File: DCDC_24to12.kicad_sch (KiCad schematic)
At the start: 26 parts, among them J1 Power_IN, J2 Power_OUT, U1 BD9F800MUX-ZE2

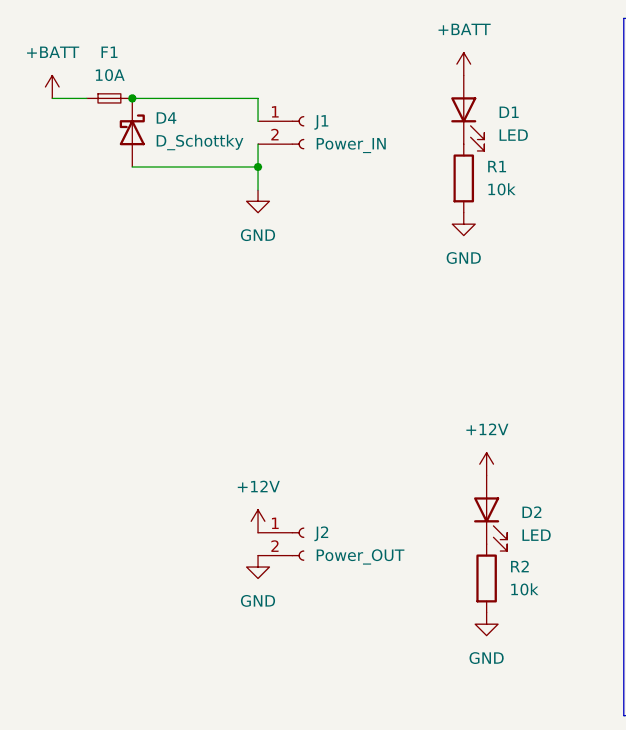
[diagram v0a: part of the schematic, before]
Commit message: XT60をヨコに変更、ピン順序修正
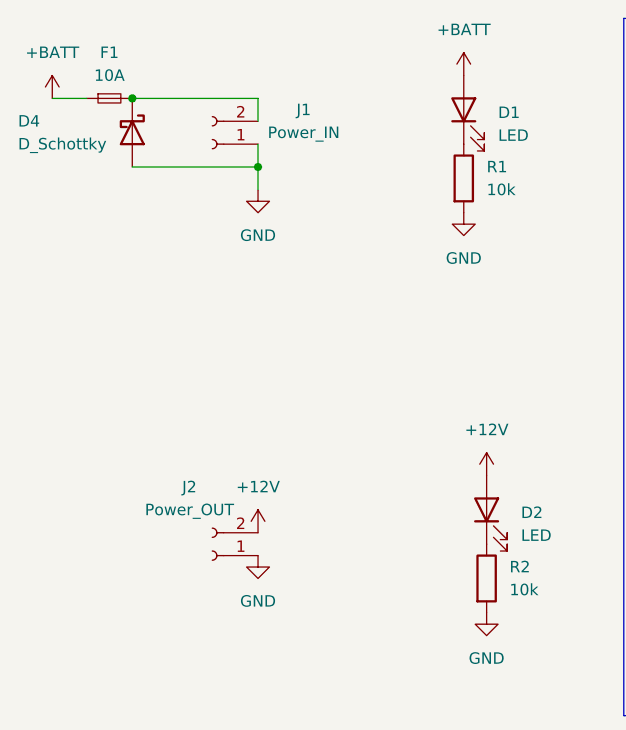
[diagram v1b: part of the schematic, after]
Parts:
- J1: footprint Connector_AMASS:AMASS_XT60-M_1x02_P7.20mm_Vertical -> Connector_AMASS:AMASS_XT60PW-M_1x02_P7.20mm_Horizontal
- J2: footprint Connector_AMASS:AMASS_XT60-F_1x02_P7.20mm_Vertical -> Connector_AMASS:AMASS_XT60PW-F_1x02_P7.20mm_Horizontal
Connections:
- net +12V: now also J2.2 (Pin_2); no longer J2.1 (Pin_1)
- net GND: now also J1.1 (Pin_1), J2.1 (Pin_1); no longer J1.2 (Pin_2), J2.2 (Pin_2)
- net at D4.1 (K), F1.2: now also J1.2 (Pin_2); no longer J1.1 (Pin_1)
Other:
- moved on the sheet: J1, J2
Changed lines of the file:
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@@
 	(symbol
 		(lib_id "Connector:Conn_01x02_Socket")
-		(at 50.8 78.74 0)
-		(unit 1)
-		(exclude_from_sim no)
-		(in_bom yes)
-		(on_board yes)
-		(dnp no)
-		(fields_autoplaced yes)
+		(at 40.64 81.28 180)
+		(unit 1)
+		(exclude_from_sim no)
+		(in_bom yes)
+		(on_board yes)
+		(dnp no)
 		(property "Reference" "J1"
-			(at 52.07 78.7399 0)
-			(effects
-				(font
-					(size 1.27 1.27)
-				)
-				(justify left)
+			(at 50.8 77.47 0)
+			(effects
+				(font
+					(size 1.27 1.27)
+				)
 			)
 		)
 		(property "Value" "Power_IN"
-			(at 52.07 81.2799 0)
-			(effects
-				(font
-					(size 1.27 1.27)
-				)
-				(justify left)
-			)
-		)
-		(property "Footprint" "Connector_AMASS:AMASS_XT60-M_1x02_P7.20mm_Vertical"
-			(at 50.8 78.74 0)
+			(at 50.8 80.01 0)
+			(effects
+				(font
+					(size 1.27 1.27)
+				)
+			)
+		)
+		(property "Footprint" "Connector_AMASS:AMASS_XT60PW-M_1x02_P7.20mm_Horizontal"
+			(at 40.64 81.28 0)
 			(effects
 				(font
@@
 		)
 		(property "Datasheet" "~"
-			(at 50.8 78.74 0)
+			(at 40.64 81.28 0)
 			(effects
 				(font
@@
 		)
 		(property "Description" "Generic connector, single row, 01x02, script generated"
-			(at 50.8 78.74 0)
+			(at 40.64 81.28 0)
 			(effects
 				(font
@@
 		(on_board yes)
 		(dnp no)
-		(fields_autoplaced yes)
 		(property "Reference" "D4"
-			(at 34.29 78.4224 90)
+			(at 19.05 78.74 90)
 			(effects
 				(font
@@
 		)
 		(property "Value" "D_Schottky"
-			(at 34.29 80.9624 90)
+			(at 19.05 81.28 90)
 			(effects
 				(font
@@
 	(symbol
 		(lib_id "Connector:Conn_01x02_Socket")
-		(at 50.8 124.46 0)
-		(unit 1)
-		(exclude_from_sim no)
-		(in_bom yes)
-		(on_board yes)
-		(dnp no)
-		(fields_autoplaced yes)
+		(at 40.64 127 180)
+		(unit 1)
+		(exclude_from_sim no)
+		(in_bom yes)
+		(on_board yes)
+		(dnp no)
 		(property "Reference" "J2"
-			(at 52.07 124.4599 0)
-			(effects
-				(font
-					(size 1.27 1.27)
-				)
-				(justify left)
+			(at 38.1 119.38 0)
+			(effects
+				(font
+					(size 1.27 1.27)
+				)
 			)
 		)
 		(property "Value" "Power_OUT"
-			(at 52.07 126.9999 0)
-			(effects
-				(font
-					(size 1.27 1.27)
-				)
-				(justify left)
-			)
-		)
-		(property "Footprint" "Connector_AMASS:AMASS_XT60-F_1x02_P7.20mm_Vertical"
-			(at 50.8 124.46 0)
+			(at 38.1 121.92 0)
+			(effects
+				(font
+					(size 1.27 1.27)
+				)
+			)
+		)
+		(property "Footprint" "Connector_AMASS:AMASS_XT60PW-F_1x02_P7.20mm_Horizontal"
+			(at 40.64 127 0)
 			(effects
 				(font
@@
 		)
 		(property "Datasheet" "~"
-			(at 50.8 124.46 0)
+			(at 40.64 127 0)
 			(effects
 				(font
@@
 		)
 		(property "Description" "Generic connector, single row, 01x02, script generated"
-			(at 50.8 124.46 0)
-			(effects
-				(font
+			(at 40.64 127 0)
+			(effects
+				(font

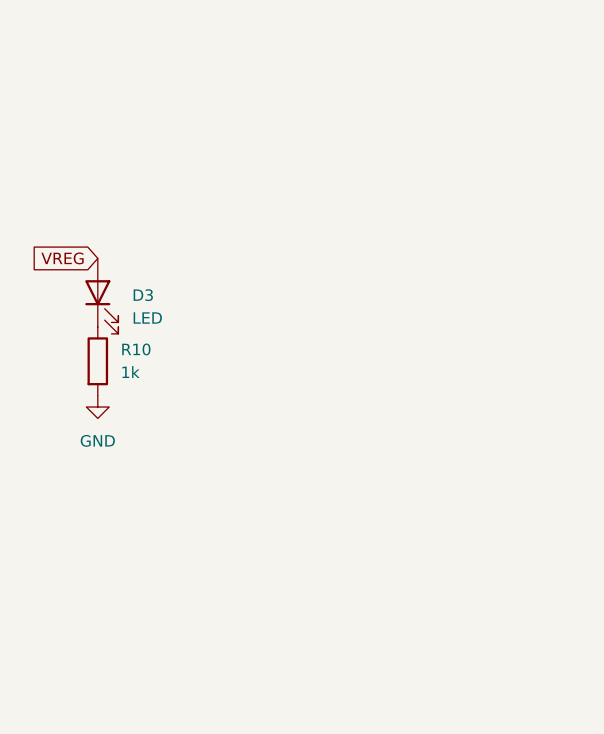
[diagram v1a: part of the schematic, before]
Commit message: 2x25pinMILコネクタ対応
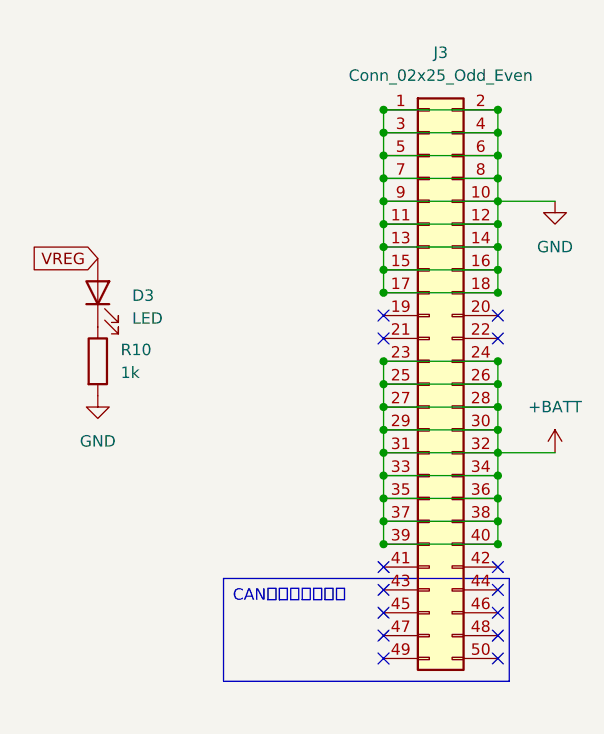
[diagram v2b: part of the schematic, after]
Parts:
- added J3: Conn_02x25_Odd_Even, Library:MD_Connecter_2×25_P2.54mm, symbol Connector_Generic:Conn_02x25_Odd_Even
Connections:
- net +BATT: now also J3.23 (Pin_23), J3.24 (Pin_24), J3.25 (Pin_25), J3.26 (Pin_26), J3.27 (Pin_27), J3.28 (Pin_28), J3.29 (Pin_29), J3.30 (Pin_30), J3.31 (Pin_31), J3.32 (Pin_32), J3.33 (Pin_33), J3.34 (Pin_34), J3.35 (Pin_35), J3.36 (Pin_36), J3.37 (Pin_37), J3.38 (Pin_38), J3.39 (Pin_39), J3.40 (Pin_40)
- net GND: now also J3.1 (Pin_1), J3.10 (Pin_10), J3.11 (Pin_11), J3.12 (Pin_12), J3.13 (Pin_13), J3.14 (Pin_14), J3.15 (Pin_15), J3.16 (Pin_16), J3.17 (Pin_17), J3.18 (Pin_18), J3.2 (Pin_2), J3.3 (Pin_3), J3.4 (Pin_4), J3.5 (Pin_5), J3.6 (Pin_6), J3.7 (Pin_7), J3.8 (Pin_8), J3.9 (Pin_9)
- no-connect marks 0 -> 14

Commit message: あれこれ
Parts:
- D1: renamed from D4; footprint Diode_SMD:D_SOD-123F -> Diode_SMD:D_SMB
- renumbered C4 to C2, C5 to C3, C2 to C4, C6 to C5, C3 to C6, D1 to D2, D2 to D3, D3 to D4, R5 to R4, R9 to R5, R4 to R6, R6 to R7, R7 to R8, R8 to R9
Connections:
- net +BATT: now also J3.12 (Pin_12), J3.14 (Pin_14), J3.16 (Pin_16), J3.18 (Pin_18), J3.20 (Pin_20), J3.22 (Pin_22); no longer J3.23 (Pin_23), J3.25 (Pin_25), J3.27 (Pin_27), J3.29 (Pin_29), J3.30 (Pin_30), J3.31 (Pin_31), J3.32 (Pin_32), J3.33 (Pin_33), J3.34 (Pin_34), J3.35 (Pin_35), J3.36 (Pin_36), J3.37 (Pin_37), J3.38 (Pin_38), J3.39 (Pin_39), J3.40 (Pin_40)
- net GND: now also J3.34 (Pin_34), J3.36 (Pin_36), J3.38 (Pin_38), J3.40 (Pin_40), J3.42 (Pin_42), J3.44 (Pin_44), J3.46 (Pin_46), J3.48 (Pin_48), J3.50 (Pin_50); no longer J3.1 (Pin_1), J3.10 (Pin_10), J3.11 (Pin_11), J3.12 (Pin_12), J3.13 (Pin_13), J3.14 (Pin_14), J3.15 (Pin_15), J3.16 (Pin_16), J3.17 (Pin_17), J3.18 (Pin_18), J3.2 (Pin_2), J3.3 (Pin_3), J3.4 (Pin_4), J3.5 (Pin_5), J3.6 (Pin_6), J3.7 (Pin_7), J3.8 (Pin_8), J3.9 (Pin_9)
- net at J3.19 (Pin_19): now also J3.11 (Pin_11), J3.13 (Pin_13), J3.15 (Pin_15), J3.17 (Pin_17), J3.21 (Pin_21), J3.23 (Pin_23), J3.25 (Pin_25), J3.27 (Pin_27)
- net at J3.41 (Pin_41): now also J3.33 (Pin_33), J3.35 (Pin_35), J3.37 (Pin_37), J3.39 (Pin_39), J3.43 (Pin_43), J3.45 (Pin_45), J3.47 (Pin_47), J3.49 (Pin_49)

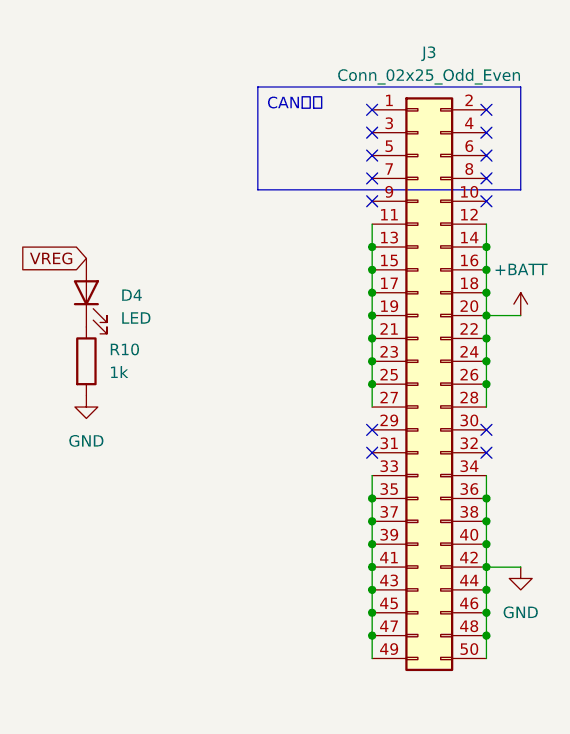
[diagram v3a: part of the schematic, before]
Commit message: MILコネクタばいばい
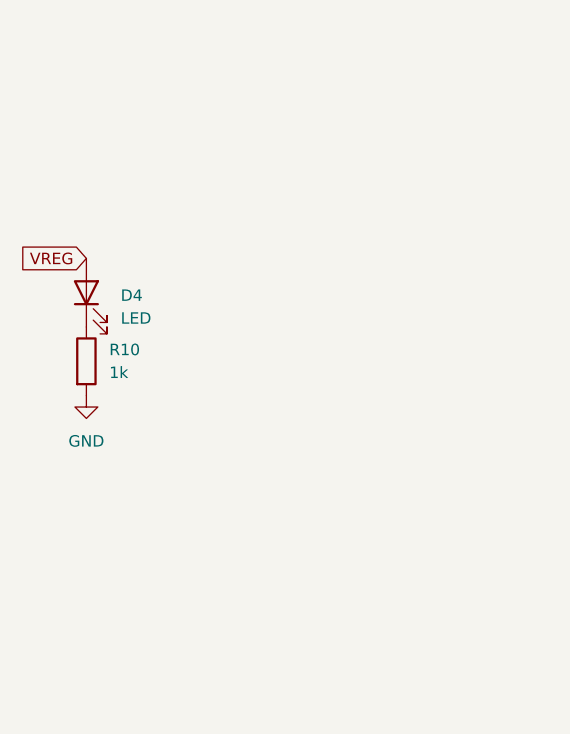
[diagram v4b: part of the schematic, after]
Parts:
- removed J3: Conn_02x25_Odd_Even, Library:MD_Connecter_2×25_P2.54mm, symbol Connector_Generic:Conn_02x25_Odd_Even
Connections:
- no-connect marks 14 -> 0

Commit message: すごい修正
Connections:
- net +BATT: now also D1.1 (K)
- net at F1.2, J1.2 (Pin_2): no longer D1.1 (K)
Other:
- moved on the sheet: F1
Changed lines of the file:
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@@
 	)
 	(junction
-		(at 31.75 76.2)
+		(at 157.48 96.52)
 		(diameter 0)
 		(color 0 0 0 0)
 	)
 	(junction
-		(at 157.48 96.52)
+		(at 167.64 138.43)
 		(diameter 0)
 		(color 0 0 0 0)
 	)
 	(junction
-		(at 167.64 138.43)
+		(at 31.75 76.2)
 		(diameter 0)
 		(color 0 0 0 0)
@@
 	(wire
 		(pts
+			(xy 36.83 76.2) (xy 45.72 76.2)
+		)
+		(stroke
+			(width 0)
+			(type default)
+		)
+	)
+	(wire
+		(pts
 			(xy 97.79 93.98) (xy 97.79 96.52)
 		)
@@
 	(wire
 		(pts
-			(xy 22.86 76.2) (xy 26.67 76.2)
+			(xy 22.86 76.2) (xy 31.75 76.2)
 		)
 		(stroke
@@
 	(wire
 		(pts
-			(xy 45.72 76.2) (xy 31.75 76.2)
-		)
-		(stroke
-			(width 0)
-			(type default)
-		)
-	)
-	(wire
-		(pts
 			(xy 147.32 88.9) (xy 157.48 88.9)
 		)
@@
 	(symbol
 		(lib_id "Device:Fuse_Small")
-		(at 29.21 76.2 0)
+		(at 34.29 76.2 0)
 		(unit 1)
 		(exclude_from_sim no)
@@
 		(fields_autoplaced yes)
 		(property "Reference" "F1"
-			(at 29.21 71.12 0)
+			(at 34.29 71.12 0)
 			(effects
 				(font
@@
 		)
 		(property "Value" "10A"
-			(at 29.21 73.66 0)
+			(at 34.29 73.66 0)
 			(effects
 				(font
@@
 		)
 		(property "Footprint" "FUSE_3557:FUSE_3557-2"
-			(at 29.21 76.2 0)
+			(at 34.29 76.2 0)
 			(effects
 				(font
@@
 		)
 		(property "Datasheet" "~"
-			(at 29.21 76.2 0)
+			(at 34.29 76.2 0)
 			(effects
 				(font
@@
 		)
 		(property "Description" "Fuse, small symbol"
-			(at 29.21 76.2 0)
+			(at 34.29 76.2 0)
 			(effects
 				(font

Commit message: 穴追加 場所がねぇ
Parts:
- added H1, H2: MountingHole, MountingHole:MountingHole_3.2mm_M3_Pad_Via, symbol Mechanical:MountingHole
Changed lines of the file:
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@@
+	)
+	(symbol
+		(lib_id "Mechanical:MountingHole")
+		(at 71.12 166.37 0)
+		(unit 1)
+		(exclude_from_sim yes)
+		(in_bom no)
+		(on_board yes)
+		(dnp no)
+		(fields_autoplaced yes)
+		(property "Reference" "H2"
+			(at 73.66 165.0999 0)
+			(effects
+				(font
+					(size 1.27 1.27)
+				)
+				(justify left)
+			)
+		)
+		(property "Value" "MountingHole"
+			(at 73.66 167.6399 0)
+			(effects
+				(font
+					(size 1.27 1.27)
+				)
+				(justify left)
+			)
+		)
+		(property "Footprint" "MountingHole:MountingHole_3.2mm_M3_Pad_Via"
+			(at 71.12 166.37 0)
+			(effects
+				(font
+					(size 1.27 1.27)
+				)
+				(hide yes)
+			)
+		)
+		(property "Datasheet" "~"
+			(at 71.12 166.37 0)
+			(effects
+				(font
+					(size 1.27 1.27)
+				)
+				(hide yes)
+			)
+		)
+		(property "Description" "Mounting Hole without connection"
+			(at 71.12 166.37 0)
+			(effects
+				(font
+					(size 1.27 1.27)
+				)
+				(hide yes)
+			)
+		)
+		(instances
+			(project ""
+				(path "/9b31bb12-b0a4-46c2-8fe3-73cecf9f3124"
+					(reference "H2")
+					(unit 1)
+				)
+			)
+		)
 	)
 	(symbol
@@
 					(unit 1)
 				)
+			)
+		)
+	)
+	(symbol
+		(lib_id "Mechanical:MountingHole")
+		(at 71.12 157.48 0)
+		(unit 1)
+		(exclude_from_sim yes)
+		(in_bom no)
+		(on_board yes)
+		(dnp no)
+		(fields_autoplaced yes)
+		(property "Reference" "H1"
+			(at 73.66 156.2099 0)
+			(effects
+				(font
+					(size 1.27 1.27)
+				)
+				(justify left)
+			)
+		)
+		(property "Value" "MountingHole"
+			(at 73.66 158.7499 0)
+			(effects
+				(font
+					(size 1.27 1.27)
+				)
+				(justify left)
+			)
+		)
+		(property "Footprint" "MountingHole:MountingHole_3.2mm_M3_Pad_Via"
+			(at 71.12 157.48 0)
+			(effects
+				(font
+					(size 1.27 1.27)
+				)
+				(hide yes)
+			)
+		)
+		(property "Datasheet" "~"
+			(at 71.12 157.48 0)
+			(effects
+				(font
+					(size 1.27 1.27)
+				)
+				(hide yes)
+			)
+		)
+		(property "Description" "Mounting Hole without connection"
+			(at 71.12 157.48 0)
+			(effects
+				(font
+					(size 1.27 1.27)
+				)
+				(hide yes)
+			)
+		)
+		(instances
+			(project ""
+				(path "/9b31bb12-b0a4-46c2-8fe3-73cecf9f3124"
+					(reference "H1")
+					(unit 1)
+				)

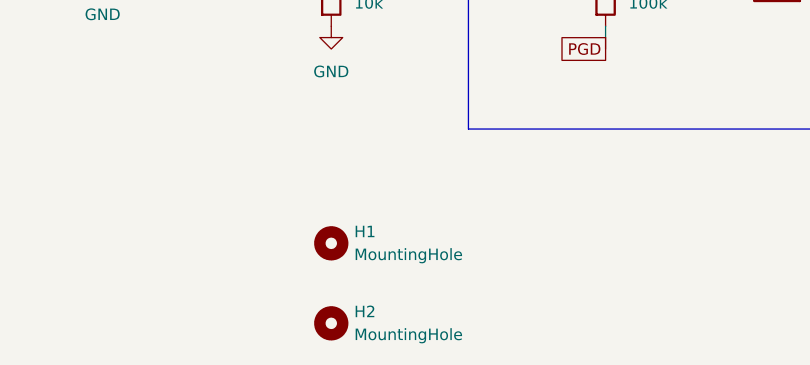
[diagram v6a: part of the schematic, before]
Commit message: 穴消したりいろいろ修正したり
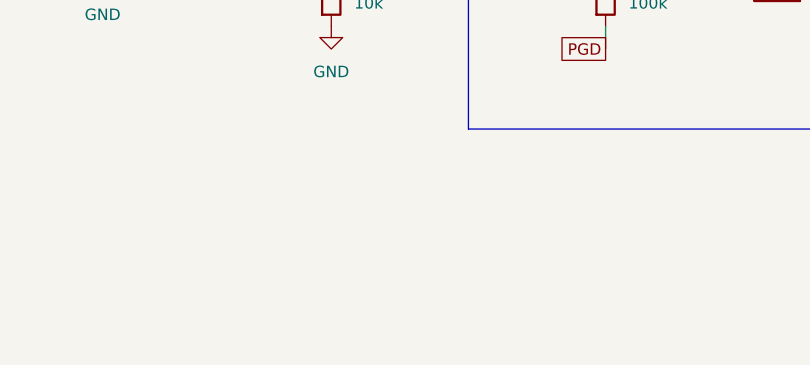
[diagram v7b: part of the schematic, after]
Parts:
- removed H1, H2: MountingHole, MountingHole:MountingHole_3.2mm_M3_Pad_Via, symbol Mechanical:MountingHole
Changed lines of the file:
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@@
-	)
-	(symbol
-		(lib_id "Mechanical:MountingHole")
-		(at 71.12 166.37 0)
-		(unit 1)
-		(exclude_from_sim yes)
-		(in_bom no)
-		(on_board yes)
-		(dnp no)
-		(fields_autoplaced yes)
-		(property "Reference" "H2"
-			(at 73.66 165.0999 0)
-			(effects
-				(font
-					(size 1.27 1.27)
-				)
-				(justify left)
-			)
-		)
-		(property "Value" "MountingHole"
-			(at 73.66 167.6399 0)
-			(effects
-				(font
-					(size 1.27 1.27)
-				)
-				(justify left)
-			)
-		)
-		(property "Footprint" "MountingHole:MountingHole_3.2mm_M3_Pad_Via"
-			(at 71.12 166.37 0)
-			(effects
-				(font
-					(size 1.27 1.27)
-				)
-				(hide yes)
-			)
-		)
-		(property "Datasheet" "~"
-			(at 71.12 166.37 0)
-			(effects
-				(font
-					(size 1.27 1.27)
-				)
-				(hide yes)
-			)
-		)
-		(property "Description" "Mounting Hole without connection"
-			(at 71.12 166.37 0)
-			(effects
-				(font
-					(size 1.27 1.27)
-				)
-				(hide yes)
-			)
-		)
-		(instances
-			(project ""
-				(path "/9b31bb12-b0a4-46c2-8fe3-73cecf9f3124"
-					(reference "H2")
-					(unit 1)
-				)
-			)
-		)
 	)
 	(symbol
@@
 					(unit 1)
 				)
-			)
-		)
-	)
-	(symbol
-		(lib_id "Mechanical:MountingHole")
-		(at 71.12 157.48 0)
-		(unit 1)
-		(exclude_from_sim yes)
-		(in_bom no)
-		(on_board yes)
-		(dnp no)
-		(fields_autoplaced yes)
-		(property "Reference" "H1"
-			(at 73.66 156.2099 0)
-			(effects
-				(font
-					(size 1.27 1.27)
-				)
-				(justify left)
-			)
-		)
-		(property "Value" "MountingHole"
-			(at 73.66 158.7499 0)
-			(effects
-				(font
-					(size 1.27 1.27)
-				)
-				(justify left)
-			)
-		)
-		(property "Footprint" "MountingHole:MountingHole_3.2mm_M3_Pad_Via"
-			(at 71.12 157.48 0)
-			(effects
-				(font
-					(size 1.27 1.27)
-				)
-				(hide yes)
-			)
-		)
-		(property "Datasheet" "~"
-			(at 71.12 157.48 0)
-			(effects
-				(font
-					(size 1.27 1.27)
-				)
-				(hide yes)
-			)
-		)
-		(property "Description" "Mounting Hole without connection"
-			(at 71.12 157.48 0)
-			(effects
-				(font
-					(size 1.27 1.27)
-				)
-				(hide yes)
-			)
-		)
-		(instances
-			(project ""
-				(path "/9b31bb12-b0a4-46c2-8fe3-73cecf9f3124"
-					(reference "H1")
-					(unit 1)
-				)

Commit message: ノーテーション改善
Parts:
- renumbered C5 to C4, C7 to C5, C4 to C6, C6 to C7, D4 to D3, D3 to D4, R3 to R1, R2 to R10, R4 to R2, R5 to R3, R6 to R4, R7 to R5, R8 to R6, R9 to R7, R1 to R8, R10 to R9
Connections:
- net +12V: now also R4.2; no longer R4.1
- net FB: now also R4.1, R5.2; no longer R4.2, R5.1
- net GND: now also R7.1; no longer R7.2
- net at R6.1: now also R7.2; no longer R5.2
- net at R6.2: now also R5.1; no longer R7.1
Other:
- moved on the sheet: C1, C2, C3, C4, C5, C6, C7, D2, D3, D4, J2, L1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
